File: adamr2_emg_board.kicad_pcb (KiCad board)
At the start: 2 copper layers, 58 x 42 mm, 8 parts, among them J1 Screw_Terminal_01x04, J2 Conn_01x02, K1 G6C-1114P-US

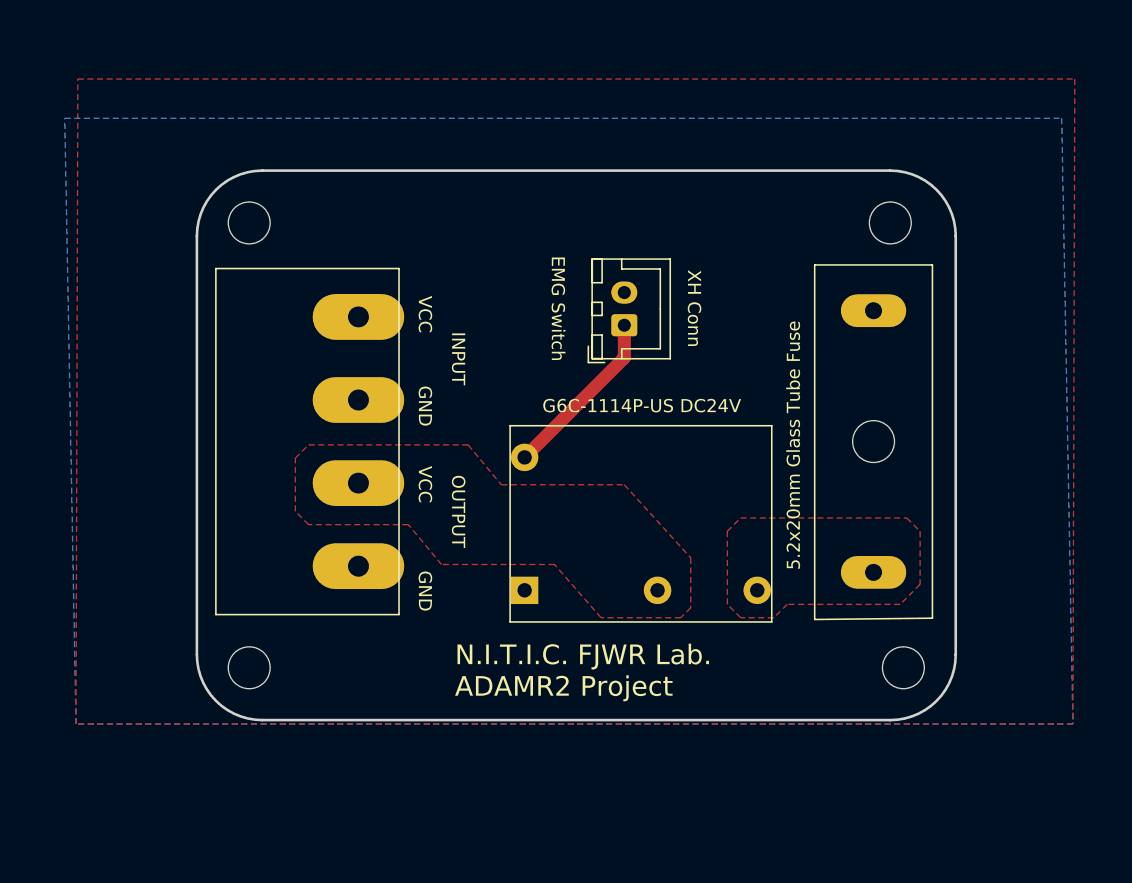
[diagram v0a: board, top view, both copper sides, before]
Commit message: Update: コンデンサを入れた
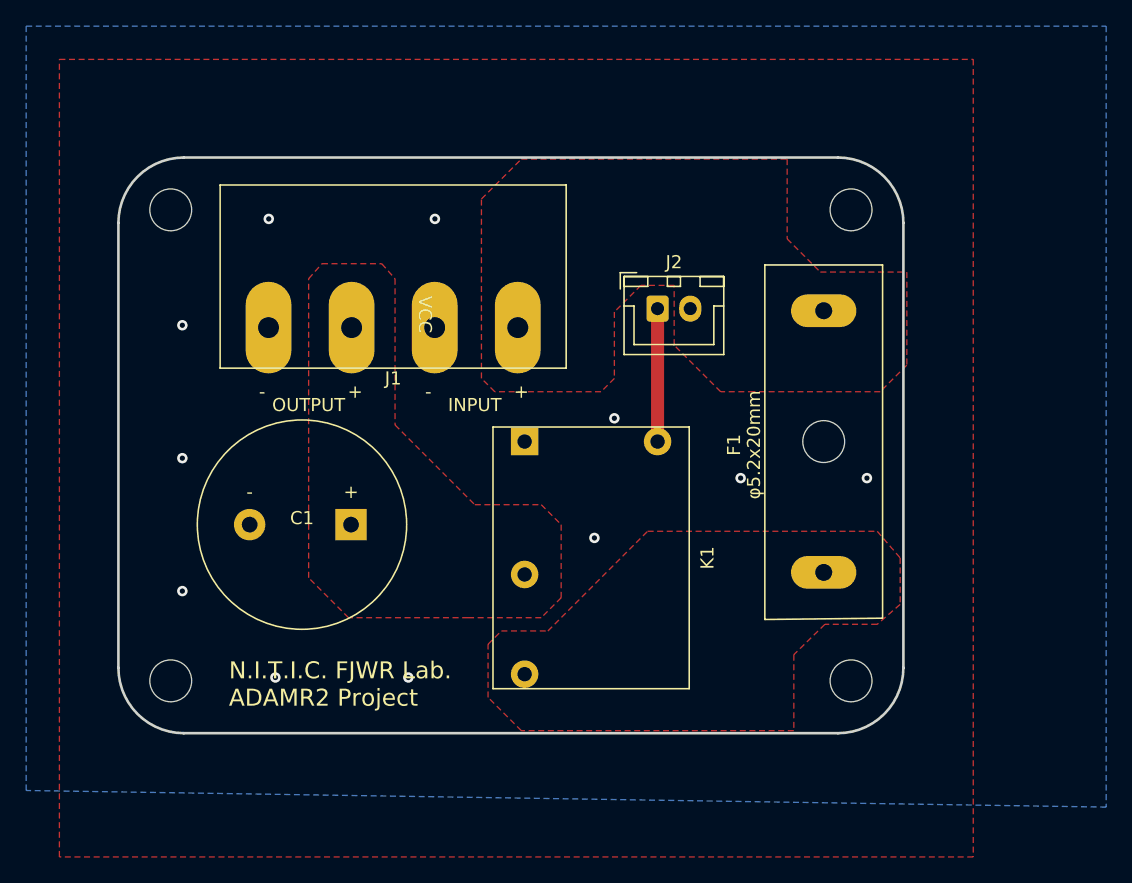
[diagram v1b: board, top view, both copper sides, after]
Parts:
- removed the REF** at (125.0, 76.0)
- removed the REF** at (125.0, 110.0)
- removed the REF** at (175.0, 110.0)
- removed the REF** at (174.0, 76.0)
- added C1: CP, adamr2_footprints:UFG1H102MHM, F.Cu at (129.0, 99.1)
- added REF**: MountingHole_3.2mm_M3, MountingHole:MountingHole_3.2mm_M3, F.Cu at (119.0, 111.0)
- added REF**: MountingHole_3.2mm_M3, MountingHole:MountingHole_3.2mm_M3, F.Cu at (119.0, 75.0)
- added REF**: MountingHole_3.2mm_M3, MountingHole:MountingHole_3.2mm_M3, F.Cu at (171.0, 111.0)
- added REF**: MountingHole_3.2mm_M3, MountingHole:MountingHole_3.2mm_M3, F.Cu at (171.0, 75.0)
- moved J1 9.10 mm to (136.0, 84.0), turned to 0 degrees
- moved K1 6.39 mm to (151.1, 102.9), turned to 90 degrees
- moved F1 3.81 mm to (168.9, 92.7)
- moved J2 2.84 mm to (156.2, 82.5), turned to 0 degrees
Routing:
- net Net-(J2-Pad1): track 13.3 -> 10.2 mm
- net GND: vias 0 -> 11
- added copper zone on F.Cu, net GND
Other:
- board size 58 x 42 mm -> 60 x 44 mm
- board text added: "+"
- board text added: "-"
- board text added: "φ5.2x20mm"
- board text removed: "5.2x20mm Glass Tube Fuse"
- board text removed: "EMG Switch"
- board text removed: "G6C-1114P-US DC24V"
- board text removed: "GND"
- board text removed: "XH Conn"
